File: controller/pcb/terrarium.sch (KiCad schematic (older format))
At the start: 56 parts, among them K1 G3MB-202P, K2 G3MB-202P, K3 G3MB-202P, Q1 S8050, Q2 S8050, Q3 S8050, SW1 RST, U1 ESP32-WROOM-32, U2 DS3231M, U5 TCA9548APWR

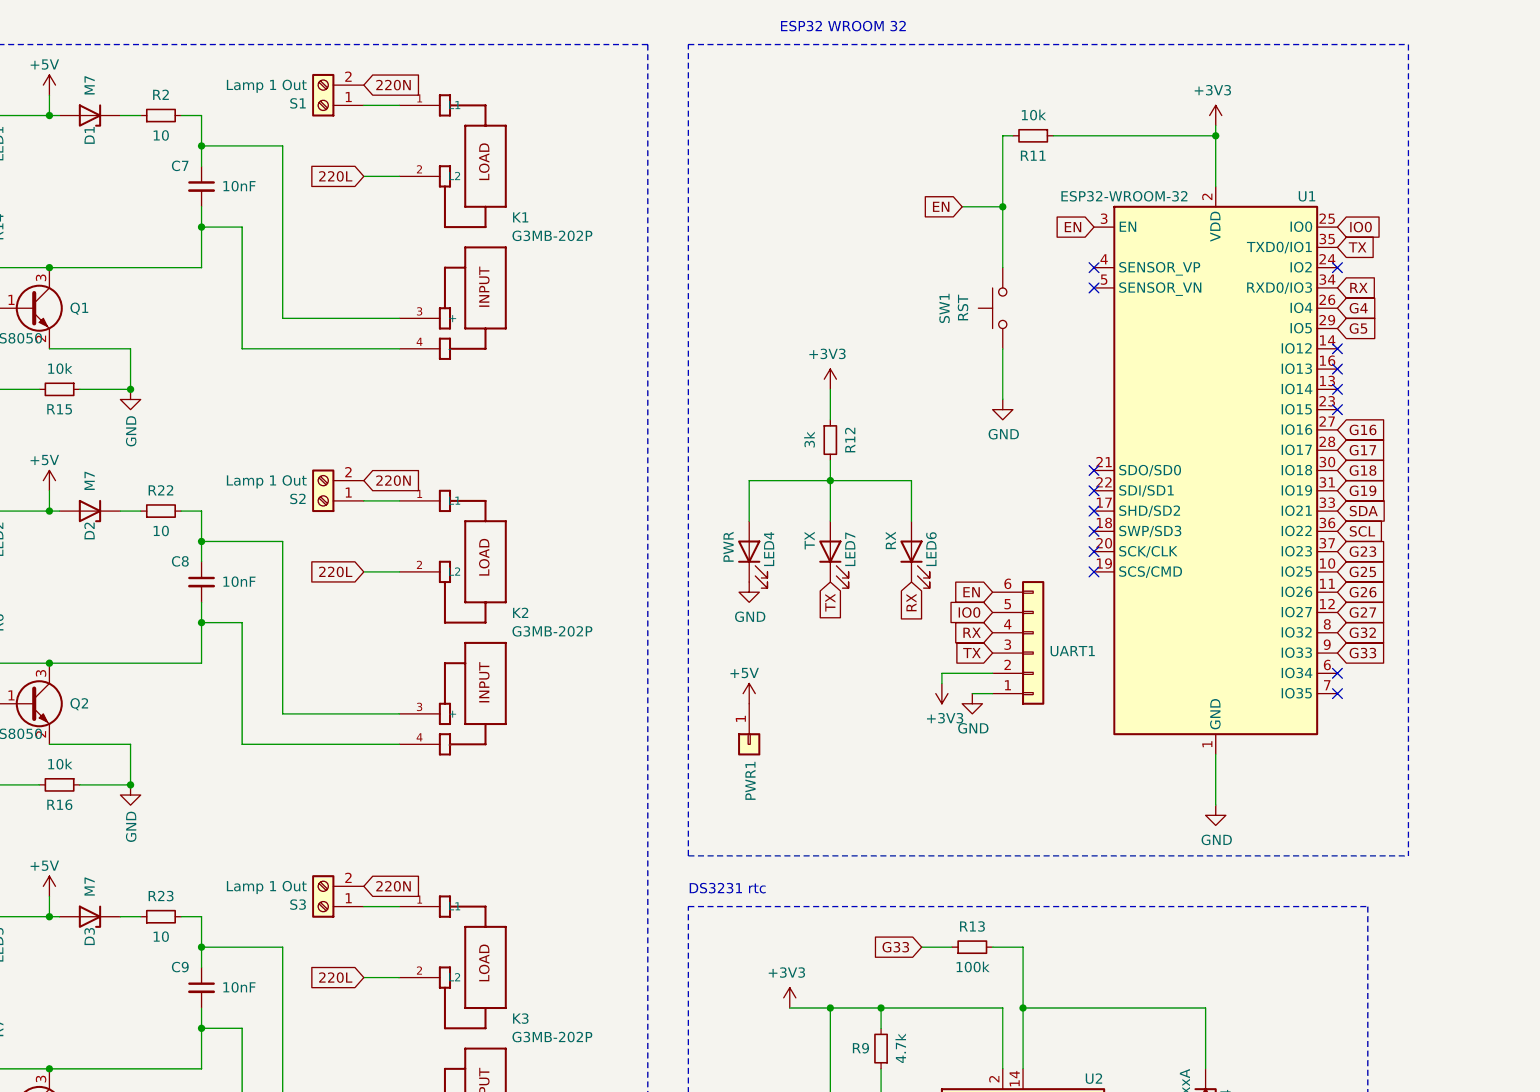
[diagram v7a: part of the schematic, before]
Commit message: move components around
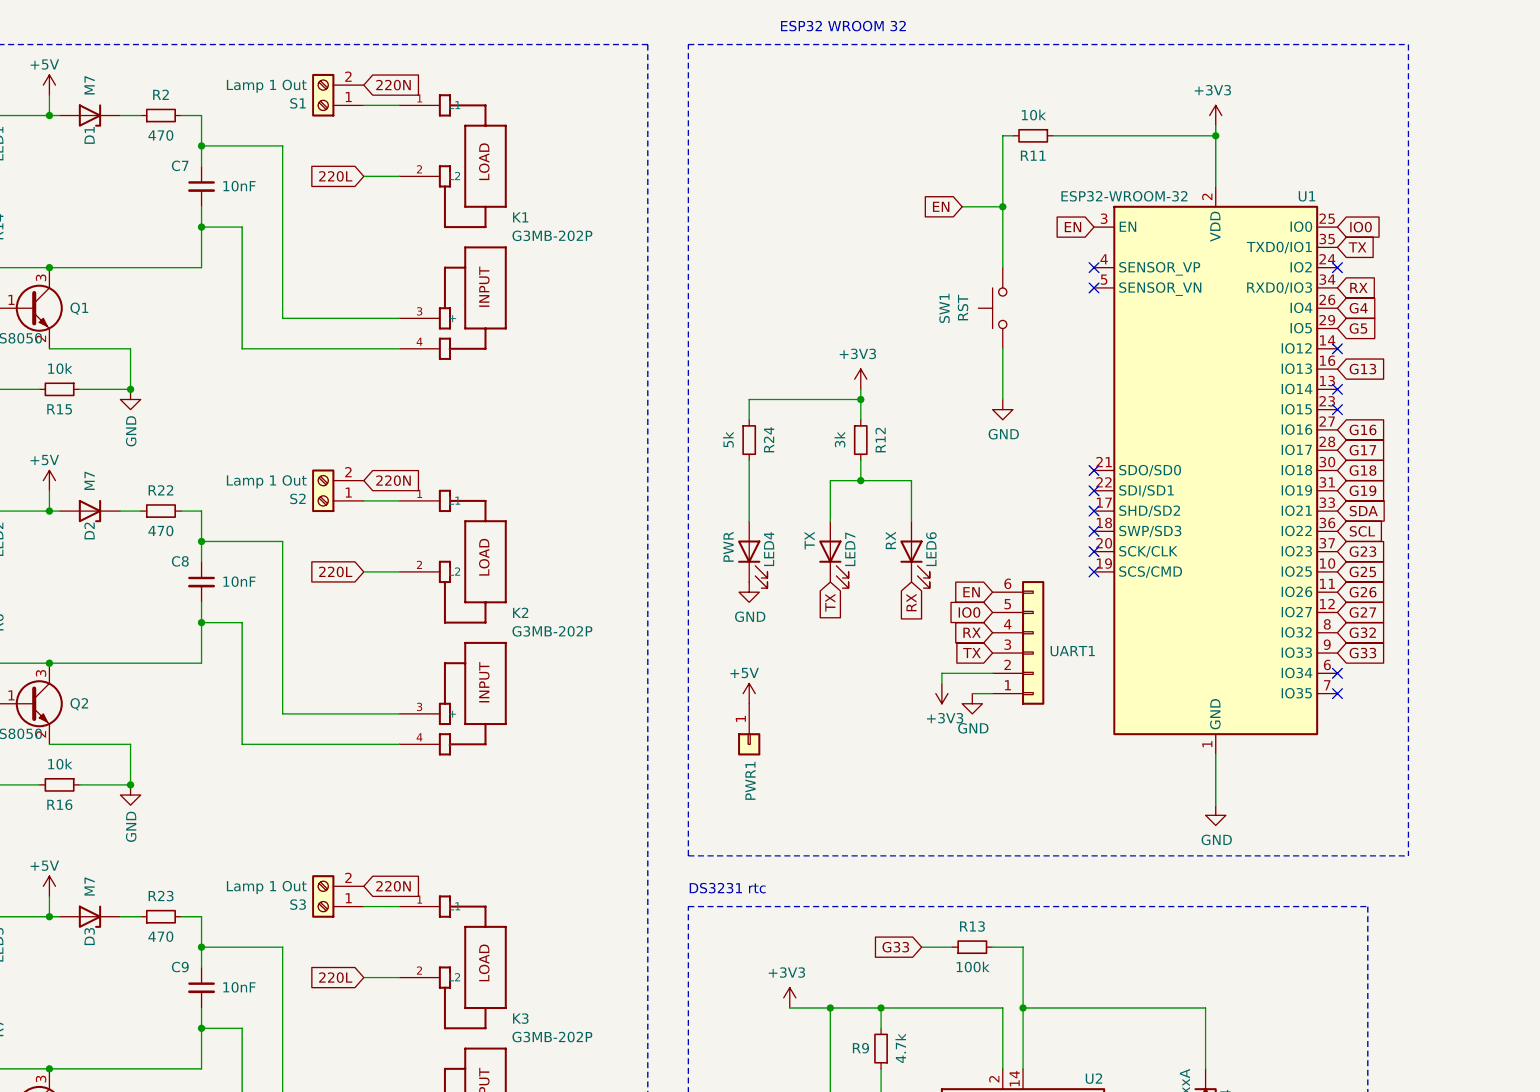
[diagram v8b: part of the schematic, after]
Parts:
- added R24: 5k, Resistor_SMD:R_1206_3216Metric, symbol Device:R_Small
- R2, R22, R23: value 10 -> 470
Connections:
- net +3V3: now also R24.1
- net G13: now reaches U1.16 (IO13)
- net at LED6.2 (A), LED7.2 (A), R12.2: no longer LED4.2 (A)
- new net: LED4.2 (A), R24.2
- no-connect marks 20 -> 19
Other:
- moved on the sheet: R12
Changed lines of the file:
@@
 NoConn ~ 10050 1800
 NoConn ~ 10050 2200
-NoConn ~ 10050 2300
 NoConn ~ 10050 2400
 NoConn ~ 10050 2500
@@
 L Device:R_Small R12
 U 1 1 624CEFE7
-P 7550 2650
-F 0 "R12" V 7650 2650 50  0000 C CNN
-F 1 "3k" V 7450 2650 50  0000 C CNN
-F 2 "Resistor_SMD:R_1206_3216Metric" H 7550 2650 50  0001 C CNN
-F 3 "~" H 7550 2650 50  0001 C CNN
-	1    7550 2650
-	1    0    0    -1
-$EndComp
-Wire Wire Line
-	7550 2750 7550 2850
-Wire Wire Line
-	7550 2400 7550 2550
+P 7700 2650
+F 0 "R12" V 7800 2650 50  0000 C CNN
+F 1 "3k" V 7600 2650 50  0000 C CNN
+F 2 "Resistor_SMD:R_1206_3216Metric" H 7700 2650 50  0001 C CNN
+F 3 "~" H 7700 2650 50  0001 C CNN
+	1    7700 2650
+	1    0    0    -1
+$EndComp
+Wire Wire Line
+	7700 2400 7700 2450
 $Comp
 L power:+3V3 #PWR0101
 U 1 1 61EFC8AF
-P 7550 2400
-F 0 "#PWR0101" H 7550 2250 50  0001 C CNN
-F 1 "+3V3" H 7565 2573 50  0000 C CNN
-F 2 "" H 7550 2400 50  0001 C CNN
-F 3 "" H 7550 2400 50  0001 C CNN
-	1    7550 2400
+P 7700 2400
+F 0 "#PWR0101" H 7700 2250 50  0001 C CNN
+F 1 "+3V3" H 7715 2573 50  0000 C CNN
+F 2 "" H 7700 2400 50  0001 C CNN
+F 3 "" H 7700 2400 50  0001 C CNN
+	1    7700 2400
 	-1   0    0    -1
 $EndComp
 Wire Wire Line
 	8500 5450 9400 5450
-Wire Wire Line
-	7550 2850 7150 2850
-Wire Wire Line
-	7150 2850 7150 3050
-Connection ~ 7550 2850
 $Comp
 L power:GND #PWR0102
@@
 $EndComp
 Wire Wire Line
-	7550 2850 7950 2850
+	7550 2850 7700 2850
 Wire Notes Line
 	700  3650 2400 3650
@@
 P 4250 1050
 F 0 "R2" V 4350 1050 50  0000 C CNN
-F 1 "10" V 4150 1050 50  0000 C CNN
+F 1 "470" V 4150 1050 50  0000 C CNN
 F 2 "Resistor_SMD:R_1206_3216Metric" H 4250 1050 50  0001 C CNN
 F 3 "~" H 4250 1050 50  0001 C CNN
@@
 P 4250 3000
 F 0 "R22" V 4350 3000 50  0000 C CNN
-F 1 "10" V 4150 3000 50  0000 C CNN
+F 1 "470" V 4150 3000 50  0000 C CNN
 F 2 "Resistor_SMD:R_1206_3216Metric" H 4250 3000 50  0001 C CNN
 F 3 "~" H 4250 3000 50  0001 C CNN
@@
 P 4250 5000
 F 0 "R23" V 4350 5000 50  0000 C CNN
-F 1 "10" V 4150 5000 50  0000 C CNN
+F 1 "470" V 4150 5000 50  0000 C CNN
 F 2 "Resistor_SMD:R_1206_3216Metric" H 4250 5000 50  0001 C CNN
 F 3 "~" H 4250 5000 50  0001 C CNN
@@
 	0    -1   -1   0
 $EndComp
+$Comp
+L Device:R_Small R24
+U 1 1 623FF425
+P 7150 2650
+F 0 "R24" V 7250 2650 50  0000 C CNN
+F 1 "5k" V 7050 2650 50  0000 C CNN
+F 2 "Resistor_SMD:R_1206_3216Metric" H 7150 2650 50  0001 C CNN
+F 3 "~" H 7150 2650 50  0001 C CNN
+	1    7150 2650
+	1    0    0    -1
+$EndComp
+Wire Wire Line
+	7150 2750 7150 3050
+Wire Wire Line
+	7700 2750 7700 2850
+Connection ~ 7700 2850
+Wire Wire Line
+	7700 2850 7950 2850
+Wire Wire Line
+	7150 2550 7150 2450
+Wire Wire Line
+	7150 2450 7700 2450
+Connection ~ 7700 2450
+Wire Wire Line
+	7700 2450 7700 2550
+Text GLabel 10050 2300 2    50   Input ~ 0
+G13
 $EndSCHEMATC
